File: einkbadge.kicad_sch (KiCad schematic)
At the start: 90 parts, among them J1 Conn_02x09_Counter_Clockwise, J3 USB_C_Receptacle_USB2.0_14P, J4 Conn_01x03, J6 lipo, Q1 AO3401A, Q6 Si1308EDL, SW21 SW_Push, SW22 SW_Push, SW23 SW_Push, SW3 SW_Push, SW4 SW_Push, SW5 SW_SPDT, SW7 SW_Push, U11 SRV05-4, U18 ST25DV04K-JFR6D3, U19 Conn, U5 RP2350_60QFN, U6 NCP1117-3.3_SOT223, U7 W25Q128JVS, U9 TP4056-42-ESOP8, Y1 ABM8-272-T3

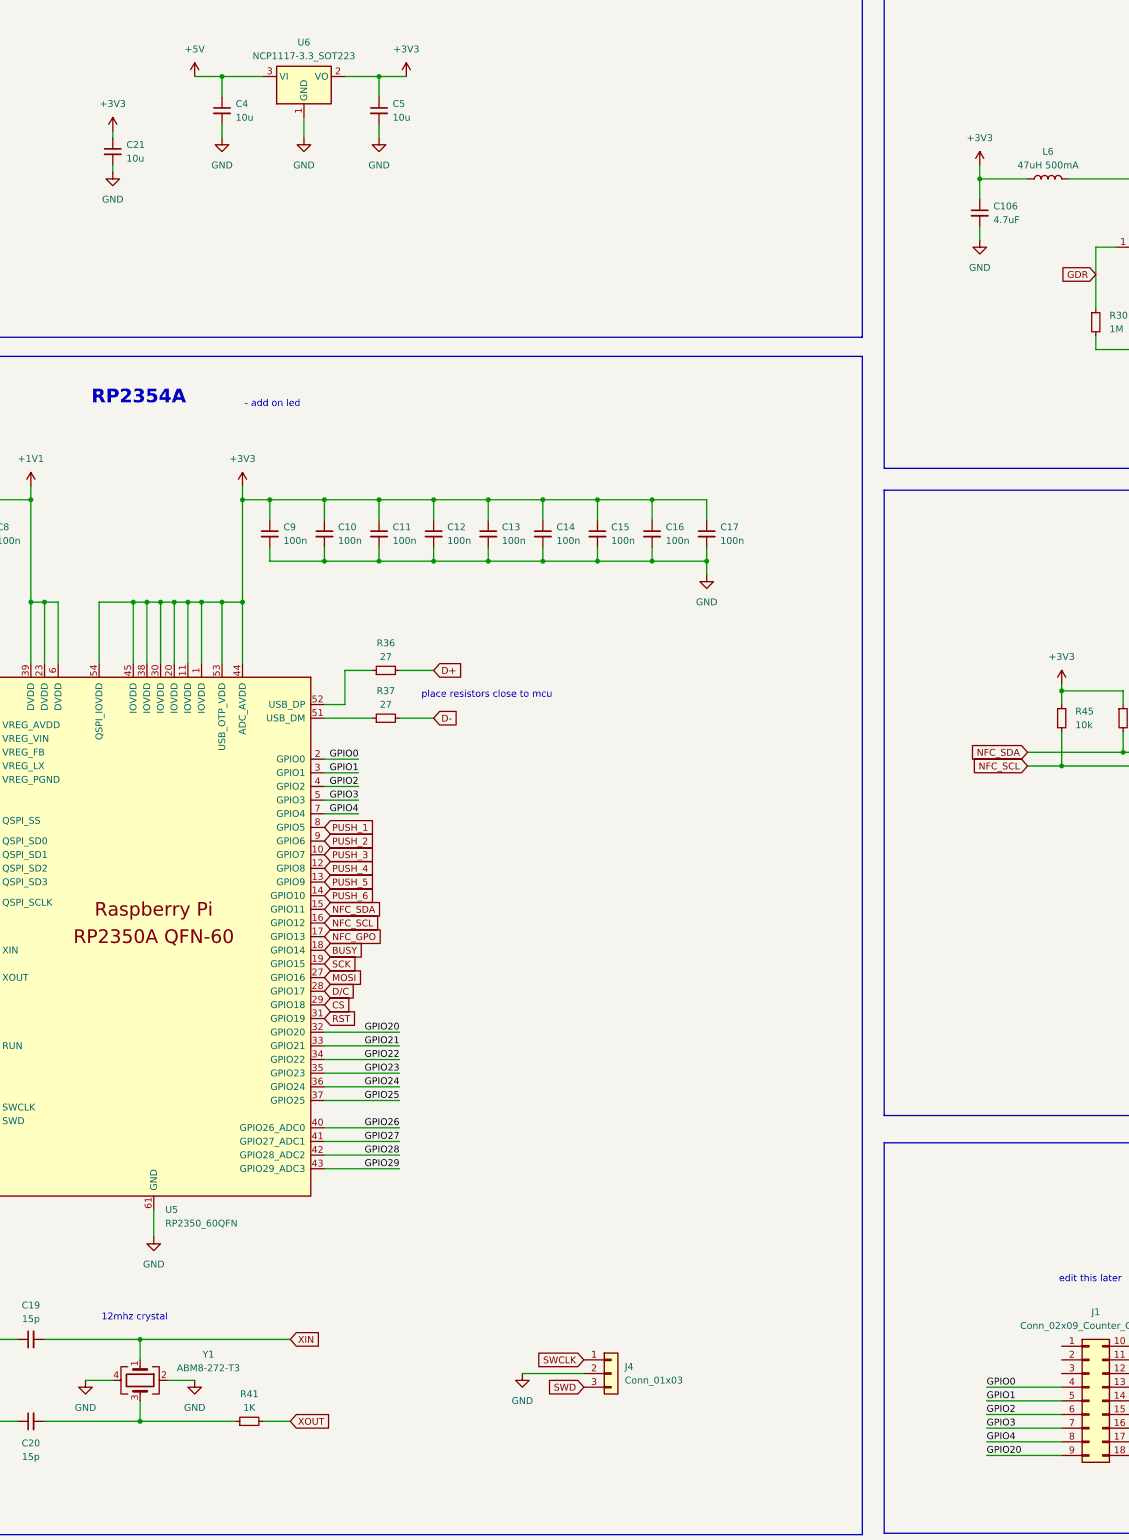
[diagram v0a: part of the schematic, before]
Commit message: update schematic
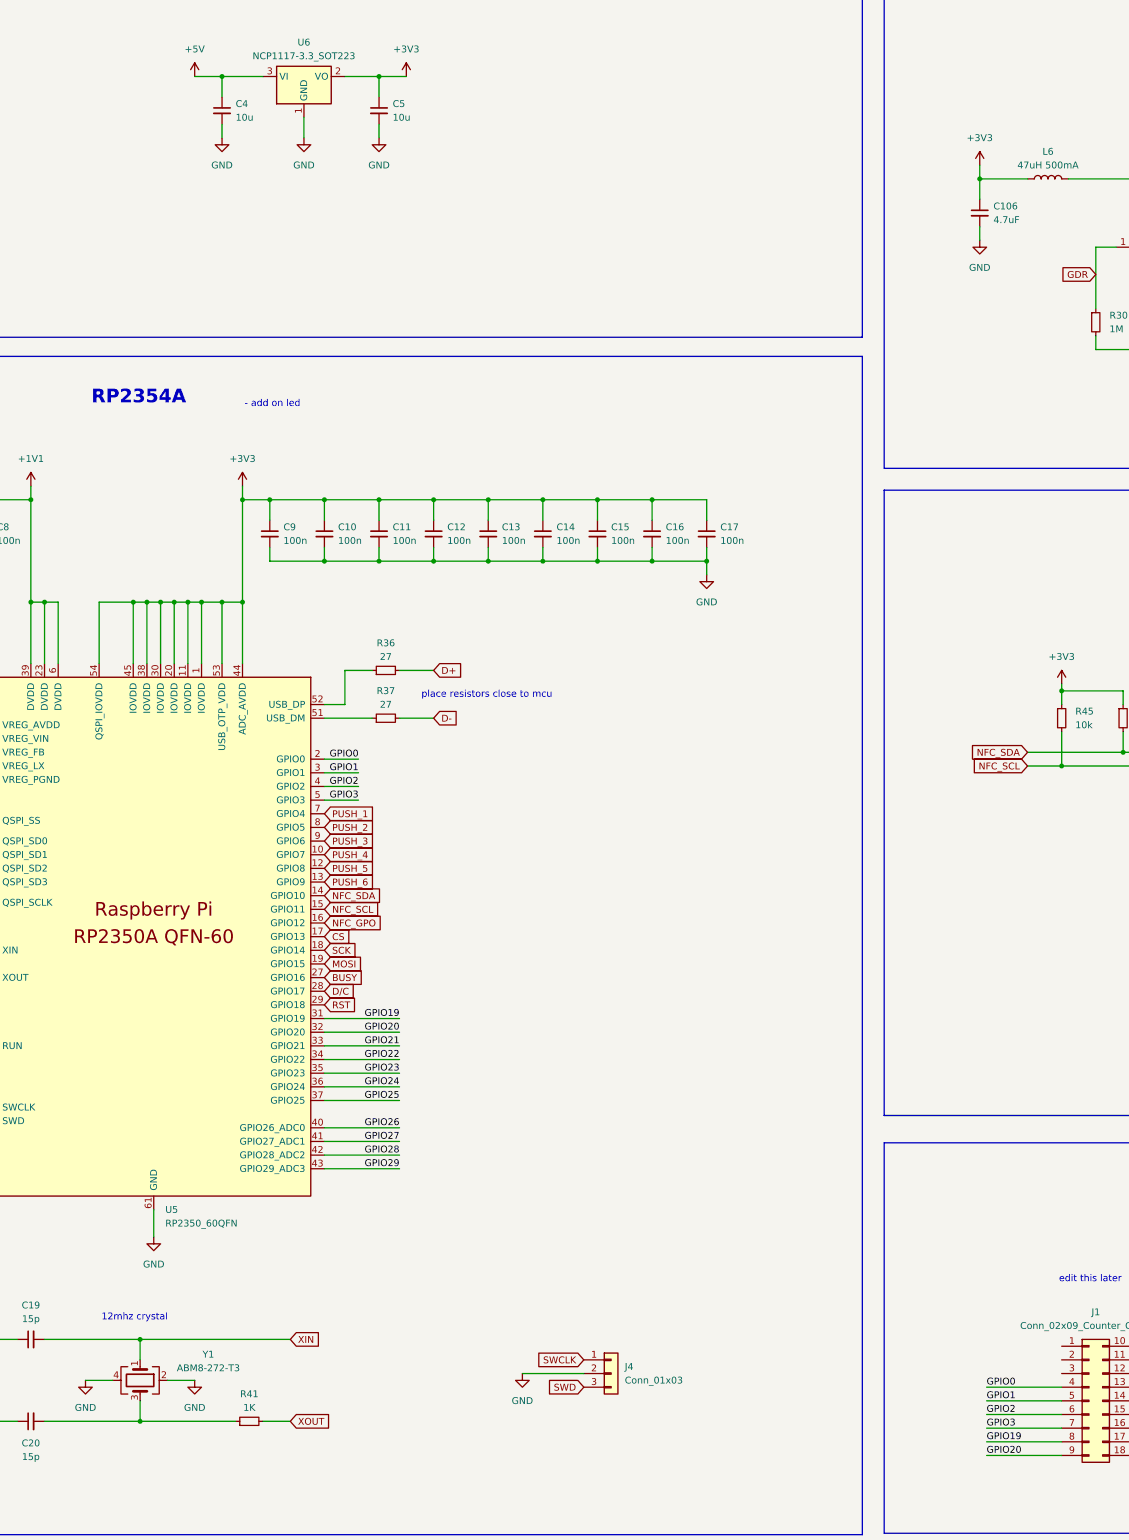
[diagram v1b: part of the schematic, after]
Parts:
- removed C21: 10u, Capacitor_SMD:C_0805_2012Metric, symbol Device:C_Small
- SW21, SW3: footprint Button_Switch_Keyboard:SW_Cherry_MX_1.00u_PCB -> Button_Switch_THT:SW_PUSH-12mm
- SW22, SW23, SW4, SW7: footprint Package_SO:TS6655TPZJ_SW_PUSH_Side -> Button_Switch_THT:SW_PUSH-12mm
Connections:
- net BUSY: now also U5.27 (GPIO16); no longer U5.18 (GPIO14)
- net CS: now also U5.17 (GPIO13); no longer U5.29 (GPIO18)
- net MOSI: now also U5.19 (GPIO15); no longer U5.27 (GPIO16)
- net NFC_GPO: now also U5.16 (GPIO12); no longer U5.17 (GPIO13)
- net NFC_SCL: now also U5.15 (GPIO11); no longer U5.16 (GPIO12)
- net NFC_SDA: now also U5.14 (GPIO10); no longer U5.15 (GPIO11)
- net PUSH_1: now also U5.7 (GPIO4); no longer U5.8 (GPIO5)
- net PUSH_2: now also U5.8 (GPIO5); no longer U5.9 (GPIO6)
- net PUSH_3: now also U5.9 (GPIO6); no longer U5.10 (GPIO7)
- net PUSH_4: now also U5.10 (GPIO7); no longer U5.12 (GPIO8)
- net PUSH_5: now also U5.12 (GPIO8); no longer U5.13 (GPIO9)
- net PUSH_6: now also U5.13 (GPIO9); no longer U5.14 (GPIO10)
- net RST: now also U5.29 (GPIO18); no longer U5.31 (GPIO19)
- net SCK: now also U5.18 (GPIO14); no longer U5.19 (GPIO15)
- net GPIO4 renamed GPIO19
- net GPIO19: now also U5.31 (GPIO19); no longer U5.7 (GPIO4)

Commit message: pcb routing almost done
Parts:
- removed C100, C101, C102, C103, C104, C95, C96, C97, C98, C99: 1uF, Capacitor_SMD:C_0402_1005Metric, symbol Device:C_Small
- removed C18: 100n, symbol Device:C_Small
- removed C22, C23: 10u, Capacitor_SMD:C_0402_1005Metric, symbol Device:C_Small
- removed D13: LED, LED_SMD:LED_0402_1005Metric, symbol Device:LED
- removed D15: MBR0530, Diode_SMD:D_SOD-123, symbol Diode:MBR0530
- removed J6: lipo, Connector_JST:JST_PH_B2B-PH-K_1x02_P2.00mm_Vertical, symbol Connector_Generic:Conn_01x02
- removed Q1: AO3401A, Package_TO_SOT_SMD:SOT-23, symbol Transistor_FET:AO3401A
- removed R39, R44: 1.5k, Resistor_SMD:R_0402_1005Metric, symbol Device:R_Small
- removed R43: 5.1k, Resistor_SMD:R_0402_1005Metric, symbol Device:R_Small
- removed SW5: SW_SPDT, Package_SO:MST-12D18G3_SPDT, symbol Switch:SW_SPDT
- removed U19: Conn, inkbadge:LCSC_1x24-1MP_P0.5mm_Horizontal, symbol inkbadge:EINK-2.9inch
- removed U7: W25Q128JVS, symbol RP2350_60QFN_minimal-cache:W25Q128JVS
- removed U9: TP4056-42-ESOP8, Package_SO:SOIC-8-1EP_3.9x4.9mm_P1.27mm_EP2.41x3.3mm_ThermalVias, symbol Battery_Management:TP4056-42-ESOP8
- added C24, C25, C26, C27, C28, C29, C30, C31, C32, C33: 1uF, Capacitor_SMD:C_0402_1005Metric, symbol Device:C_Small
- added U5: Conn, Connector_FFC-FPC:Jushuo_AFC07-S24FCA-00_1x24-1MP_P0.50_Horizontal, symbol inkbadge:EINK-2.9inch
- BOOT1, RESET1: footprint Package_SO:TS-1088-AR -> Button_Switch_SMD:SW_Push_1P1T_XKB_TS-1187A
- C1, C2: footprint Capacitor_SMD:C_0402_1005Metric -> Capacitor_SMD:C_0603_1608Metric
- D4: renamed from D24; footprint (none) -> LED_SMD:LED_0805_2012Metric
- J2: renamed from J4; footprint Connector_PinHeader_1.00mm:PinHeader_1x03_P1.00mm_Vertical -> Connector_PinHeader_2.54mm:PinHeader_1x03_P2.54mm_Vertical
- L3: renamed from L8; footprint (none) -> ant:KiCadAntenna
- SW1: renamed from SW3; footprint Button_Switch_THT:SW_PUSH-12mm -> Button_Switch_THT:SW_PUSH-12mm_Wuerth-430476085716
- SW2: renamed from SW4; footprint Button_Switch_THT:SW_PUSH-12mm -> Button_Switch_THT:SW_PUSH-12mm_Wuerth-430476085716
- SW3: renamed from SW7; footprint Button_Switch_THT:SW_PUSH-12mm -> Button_Switch_THT:SW_PUSH-12mm_Wuerth-430476085716
- SW4: renamed from SW21; footprint Button_Switch_THT:SW_PUSH-12mm -> Button_Switch_THT:SW_PUSH-12mm_Wuerth-430476085716
- SW5: renamed from SW22; footprint Button_Switch_THT:SW_PUSH-12mm -> Button_Switch_THT:SW_PUSH-12mm_Wuerth-430476085716
- SW6: renamed from SW23; footprint Button_Switch_THT:SW_PUSH-12mm -> Button_Switch_THT:SW_PUSH-12mm_Wuerth-430476085716
- renumbered C9 to C10, C10 to C11, C5 to C12, C11 to C13, C12 to C14, C13 to C15, C14 to C16, C15 to C17, C16 to C18, C17 to C19, C106 to C20, C105 to C21, C107 to C22, C108 to C23, C6 to C4, C7 to C5, C8 to C6, C19 to C7, C20 to C8, C4 to C9, D23 to D1, D21 to D2, D22 to D3, H5 to H1, H6 to H2, H7 to H3, H8 to H4, J3 to J1, J1 to J3, L6 to L2, Q6 to Q1, R34 to R1, R30 to R10, R38 to R11, R29 to R12, R31 to R13, R32 to R14, R35 to R2, R33 to R3, R40 to R4, R42 to R5, R41 to R6, R36 to R7, R37 to R8, R45 to R9, U11 to U1, U5 to U2, U6 to U3, U18 to U4
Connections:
- net +3V3: now also C25.2, U5.10 (VDDIO), U5.9 (VCI)
- net BUSY: now also U5.16 (BUSY)
- net CS: now also U5.13 (~{CS})
- net D/C: now also U5.14 (~{D/C})
- net GDR: now also U5.23 (GDR)
- net GND: now also C24.1, C25.1, C26.1, C27.1, C28.1, C29.1, C30.1, C31.1, C32.1, C33.1, U5.17 (BS1), U5.8 (VSS), U5.MP (SHIELD)
- net MOSI: now also U5.11 (SDA)
- net PREVGH: now also C32.2, U5.4 (VGH)
- net PREVGL: now also C33.2, U5.2 (VGL)
- net PUSH_1: now also U2.10 (GPIO7); no longer U2.7 (GPIO4)
- net PUSH_2: now also U2.12 (GPIO8); no longer U2.8 (GPIO5)
- net PUSH_3: now also U2.13 (GPIO9); no longer U2.9 (GPIO6)
- net PUSH_4: now also U2.9 (GPIO6); no longer U2.10 (GPIO7)
- net PUSH_5: now also U2.8 (GPIO5); no longer U2.12 (GPIO8)
- net PUSH_6: now also U2.7 (GPIO4); no longer U2.13 (GPIO9)
- net RESE: now also U5.22 (RESE)
- net RST: now also U5.15 (~{RST})
- net SCK: now also U5.12 (SCL)
- new net: C31.2, U5.6 (VPP)
- new net: C24.2, U5.21 (VGL/NC)
- new net: C29.2, U5.1 (NC)
- new net: C26.2, U5.7 (VDD)
- new net: C30.2, U5.20 (VSH2)
- new net: C28.2, U5.3 (VSL)
- new net: C27.2, U5.5 (VSH1)
- no-connect marks 7 -> 5
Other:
- note added: "CHECK THIS FOOTPRINT"
- note removed: "FLASH"
- note removed: "LIPO CIRCUIT"
- note removed: "i hope 0402 works"
- note removed: "unpopulated if using rp2354"

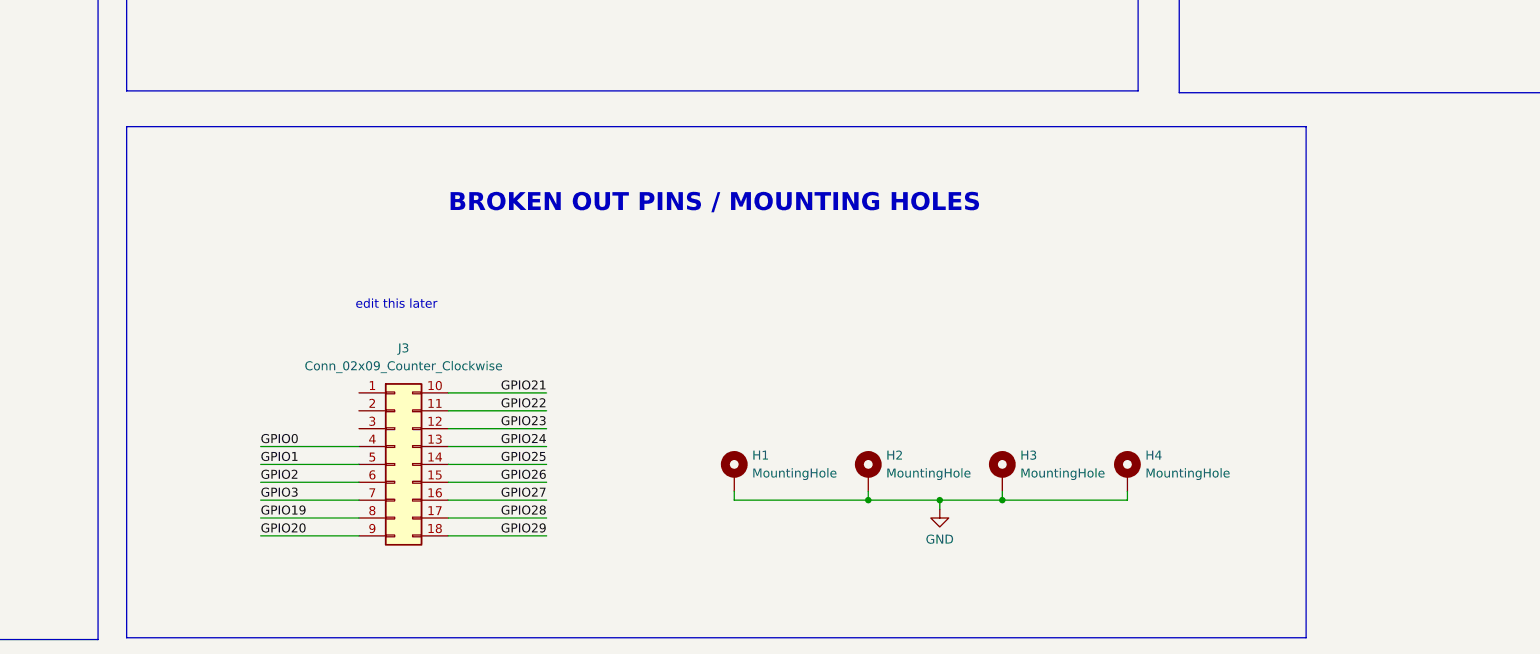
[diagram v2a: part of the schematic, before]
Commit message: pcb update (add gpio breakouts)
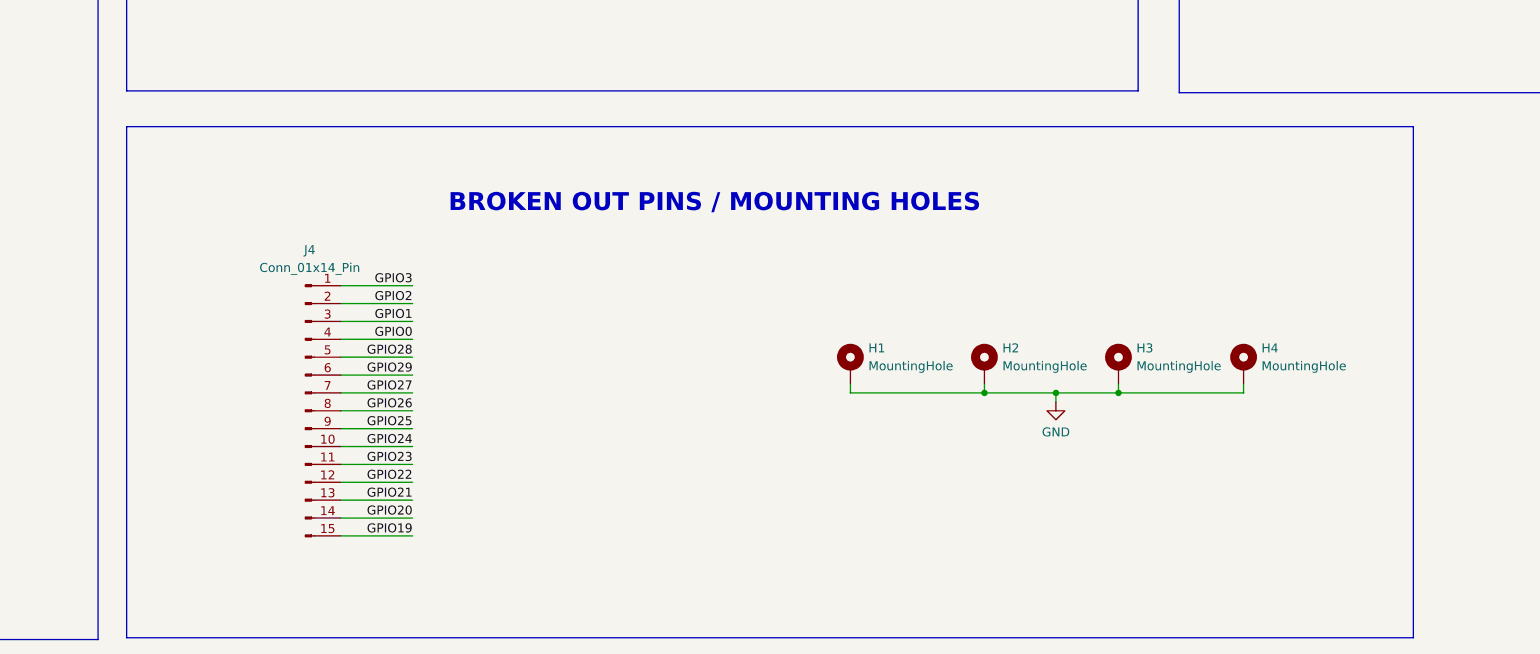
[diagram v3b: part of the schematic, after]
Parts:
- removed J3: Conn_02x09_Counter_Clockwise, symbol Connector_Generic:Conn_02x09_Top_Bottom
- added J4: Conn_01x14_Pin, Connector_PinHeader_2.54mm:PinHeader_1x15_P2.54mm_Vertical, symbol Connector:Conn_01x15_Pin
- C1, C2: footprint Capacitor_SMD:C_0603_1608Metric -> Capacitor_SMD:C_0402_1005Metric
- L1: footprint Inductor_SMD:L_0805_2012Metric -> ant:Abracon AOTA-B201610S3R3-101-T
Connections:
- net GPIO0: now also J4.4 (Pin_4)
- net GPIO1: now also J4.3 (Pin_3)
- net GPIO19: now also J4.15 (Pin_15)
- net GPIO2: now also J4.2 (Pin_2)
- net GPIO20: now also J4.14 (Pin_14)
- net GPIO21: now also J4.13 (Pin_13)
- net GPIO22: now also J4.12 (Pin_12)
- net GPIO23: now also J4.11 (Pin_11)
- net GPIO24: now also J4.10 (Pin_10)
- net GPIO25: now also J4.9 (Pin_9)
- net GPIO26: now also J4.8 (Pin_8)
- net GPIO27: now also J4.7 (Pin_7)
- net GPIO28: now also J4.5 (Pin_5)
- net GPIO29: now also J4.6 (Pin_6)
- net GPIO3: now also J4.1 (Pin_1)
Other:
- note removed: "edit this later"
- moved on the sheet: H1, H2, H3, H4
